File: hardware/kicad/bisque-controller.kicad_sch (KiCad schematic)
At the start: 49 parts, among them J1 USB-C, J2 5V_IN, J3 TC_K, J4 SSR, J5 DISPLAY, J6 NAV_SW, J7 AUX, Q1 AO3400A, Q2 AO3400A, SW1 RESET, SW2 BOOT, U1 ESP32-S3-WROOM-1-N8R2, U2 AMS1117-3.3, U3 MAX31855KASA+, U4 USBLC6-2SC6

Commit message: Replace pin headers with Molex KK-254 friction-lock headers
J5 (display), J6 (nav switch) and J7 (aux) switch from plain 2.54mm pin
headers to Molex KK-254 AE-6410 friction-lock headers, so each mating
housing is polarized and cannot be plugged in reversed. Pin positions are
unchanged (same 2.54mm row); the board was re-routed around the larger
oval pads and re-verified (ALL CHECKS PASS). Silk pin-name labels moved
out from under the deeper connector bodies, 3D renders updated with the
friction-lock body shape, BOM lists the headers plus mating housings and
crimp terminals.

Co-Authored-By: Claude Fable 5 <noreply@anthropic.com>
Claude-Session: https://claude.ai/code/session_017JbapEYPC7fC91erkTARYt
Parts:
- J5, J7: footprint Connector_PinHeader_2.54mm:PinHeader_1x08_P2.54mm_Vertical -> Connector_Molex:Molex_KK-254_AE-6410-08A_1x08_P2.54mm_Vertical
- J6: footprint Connector_PinHeader_2.54mm:PinHeader_1x06_P2.54mm_Vertical -> Connector_Molex:Molex_KK-254_AE-6410-06A_1x06_P2.54mm_Vertical
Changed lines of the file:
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@@
 			(effects (font (size 1.27 1.27)) (justify left))
 		)
-		(property "Footprint" "Connector_PinHeader_2.54mm:PinHeader_1x08_P2.54mm_Vertical" (at 39.37 214.63 0)
+		(property "Footprint" "Connector_Molex:Molex_KK-254_AE-6410-08A_1x08_P2.54mm_Vertical" (at 39.37 214.63 0)
 			(effects (font (size 1.27 1.27)) (hide yes))
 		)
@@
 			(effects (font (size 1.27 1.27)) (justify left))
 		)
-		(property "Footprint" "Connector_PinHeader_2.54mm:PinHeader_1x06_P2.54mm_Vertical" (at 76.2 214.63 0)
+		(property "Footprint" "Connector_Molex:Molex_KK-254_AE-6410-06A_1x06_P2.54mm_Vertical" (at 76.2 214.63 0)
 			(effects (font (size 1.27 1.27)) (hide yes))
 		)
@@
 			(effects (font (size 1.27 1.27)) (justify left))
 		)
-		(property "Footprint" "Connector_PinHeader_2.54mm:PinHeader_1x08_P2.54mm_Vertical" (at 111.76 214.63 0)
-			(effects (font (size 1.27 1.27)) (hide yes))
-		)
+		(property "Footprint" "Connector_Molex:Molex_KK-254_AE-6410-08A_1x08_P2.54mm_Vertical" (at 111.76 214.63 0)
+			(effects (font (size 1.27 1.27)) (hide yes))
+		)

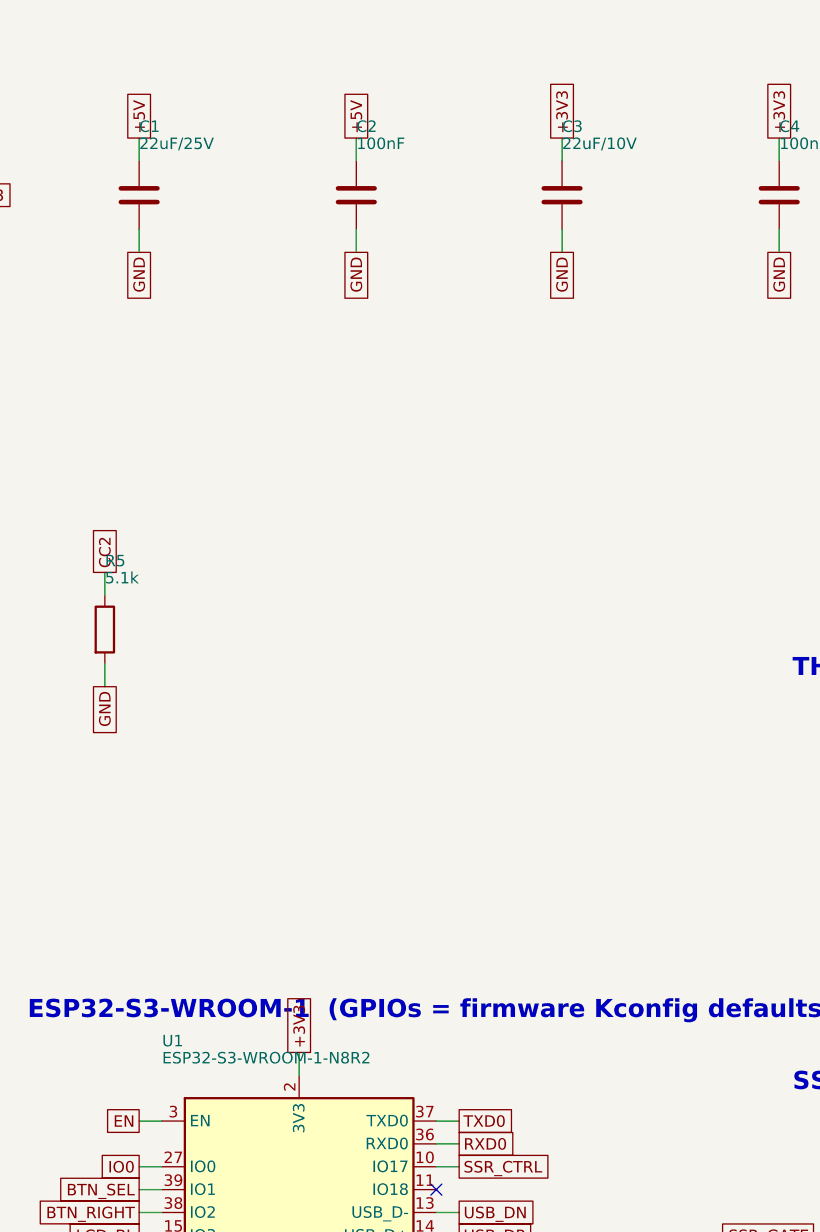
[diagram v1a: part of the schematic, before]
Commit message: Verify JLCPCB manufacturability, add assembly BOM/CPL export
- Confirm the board clears JLCPCB standard 2-layer capabilities with wide
  margins (0.25mm min track vs 0.127 limit, 0.6/0.3 vias, 0.3mm min
  drill, 100x80mm inside the cheapest <=100x100mm tier) — no upcharges.
- Fix U1 variant: firmware sdkconfig uses octal PSRAM and a 16MB OTA
  partition table, so the module must be ESP32-S3-WROOM-1-N16R8 (LCSC
  C2913202, in stock), not N8R2. IO35-37 were already NC on the board as
  octal PSRAM requires.
- Consolidate C1/C3 to one 22uF/25V 1206 part for BOM simplicity.
- New generator/gen_jlc.py emits jlcpcb/BOM.csv + CPL.csv with LCSC part
  numbers (verified ones marked; commodity parts flagged for confirmation
  in JLC's BOM matcher). Key parts verified in catalog: ESP32-S3 module,
  MAX31855KASA+T (C52028), USB-C TYPE-C-31-M-12 (C165948), AMS1117,
  AO3400A, SS34/SS14, 1N4148W and all passives as Basic parts.
- README: fabrication capability table, price expectations, and three
  assembly strategies (SMT-only recommended).

Co-Authored-By: Claude Fable 5 <noreply@anthropic.com>
Claude-Session: https://claude.ai/code/session_017JbapEYPC7fC91erkTARYt
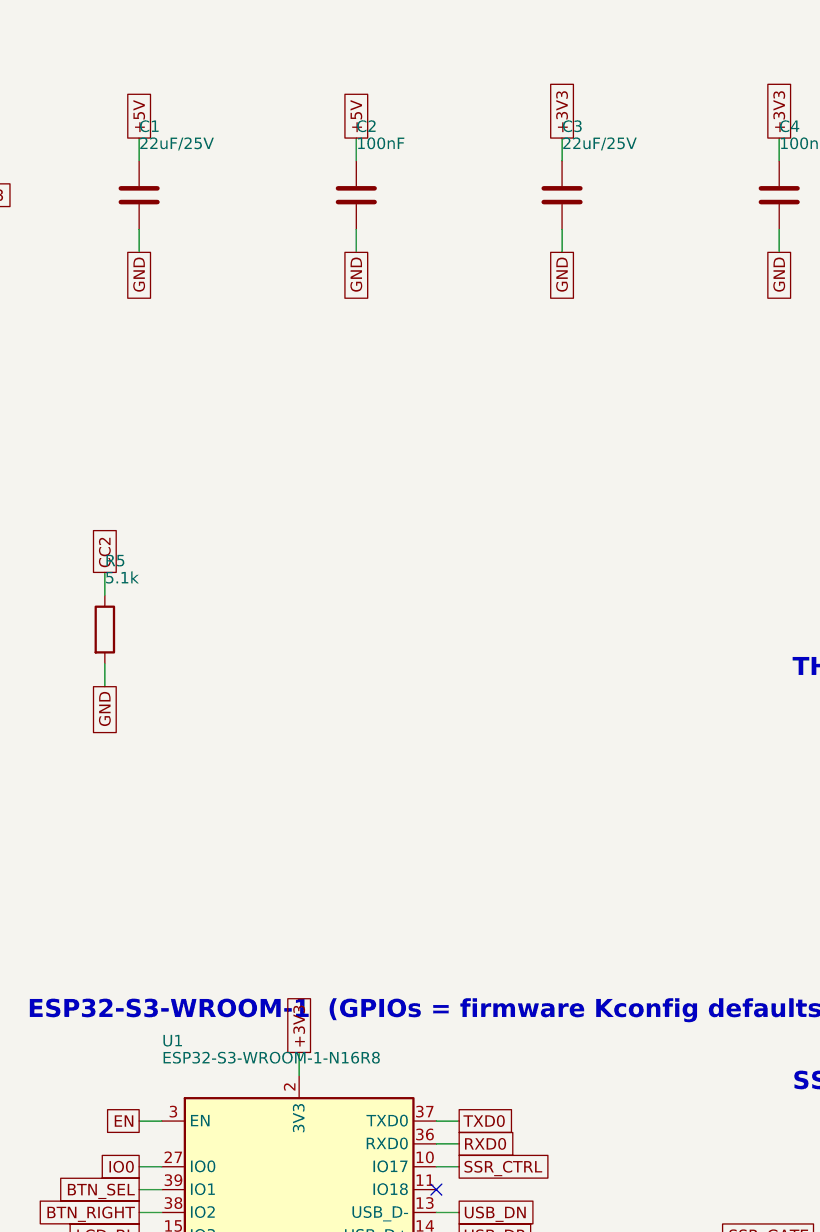
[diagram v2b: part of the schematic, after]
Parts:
- C3: value 22uF/10V -> 22uF/25V
- U1: value ESP32-S3-WROOM-1-N8R2 -> ESP32-S3-WROOM-1-N16R8
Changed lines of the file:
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@@
 			(effects (font (size 1.27 1.27)) (justify left))
 		)
-		(property "Value" "ESP32-S3-WROOM-1-N8R2" (at 154.94 135.25 0)
+		(property "Value" "ESP32-S3-WROOM-1-N16R8" (at 154.94 135.25 0)
 			(effects (font (size 1.27 1.27)) (justify left))
 		)
@@
 			(effects (font (size 1.27 1.27)) (justify left))
 		)
-		(property "Value" "22uF/10V" (at 199.39 33.65 0)
-			(effects (font (size 1.27 1.27)) (justify left))
-		)
+		(property "Value" "22uF/25V" (at 199.39 33.65 0)
+			(effects (font (size 1.27 1.27)) (justify left))
+		)

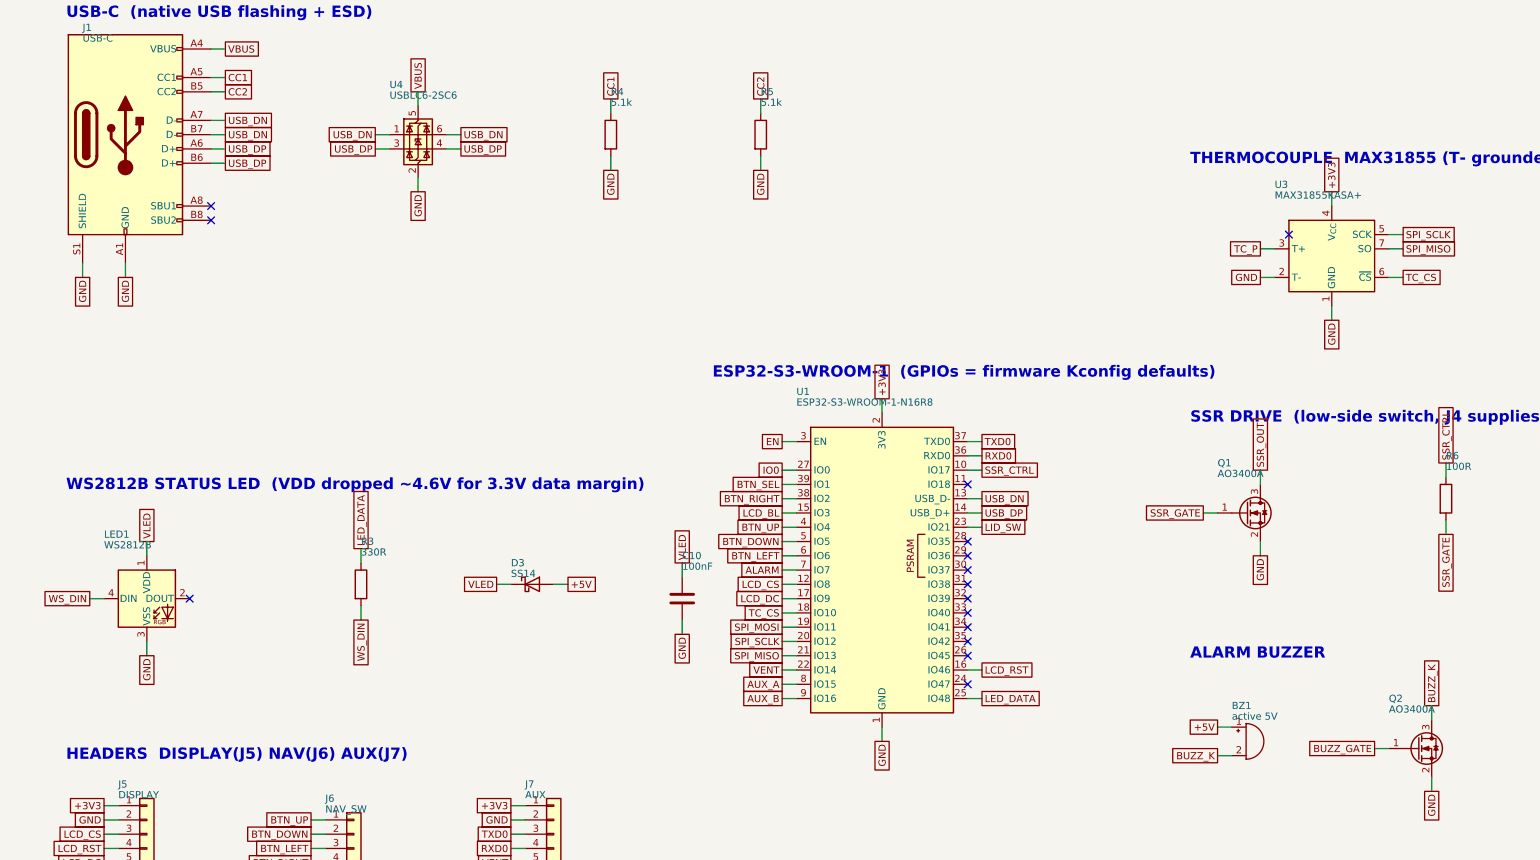
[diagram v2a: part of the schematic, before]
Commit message: Rebuild PCB and schematic through real KiCad (7.0.11)
KiCad is now installed in the build environment (Ubuntu universe; the
KiCad 9 PPA is blocked by network policy), so the project is rebuilt
through KiCad's own engine instead of hand-written file generation:

- generator/kicad_build.py constructs the board via the pcbnew Python
  API: footprints loaded from KiCad's installed system libraries, router
  obstacle model taken from the loaded pad geometry, tracks/vias/zones/
  silk added as real pcbnew objects, ground pours filled by KiCad's
  ZONE_FILLER, saved by pcbnew (KiCad 7 format, opens in 7/8/9).
- KiCad DRC (WriteDRCReport) runs as part of the build: ZERO errors,
  zero unconnected items (report committed). DRC drove real fixes my
  own checker had missed: module EP thermal vias upsized 0.2->0.3mm
  (keeps JLCPCB standard drill range), hole-to-hole clearance added to
  the router's via placement, solid pour connections where thermal
  spokes starved, explicit GND stubs routed for every SMD GND pad plus
  automatic pour-island healing (stitch via dropped into any isolated
  fill fragment), and a pre-seeded escape for U4's boxed-in GND pin.
- Schematic regenerated in KiCad 7 format from the system symbol
  libraries and validated by round-trip: kicad-cli exports the netlist
  and check_netlist.py diffs it against design.py - 42 nets, 0
  mismatches.
- Fabrication outputs exported with kicad-cli and committed: gerbers +
  Excellon drill + job file (gerbers/), schematic + board PDFs (pdf/).
- .kicad_pro rewritten by pcbnew as a native project with full rule
  severities; 2D/3D previews regenerated; README workflow updated.
  gen_pcb.py retained as a KiCad-free fallback generator.

Co-Authored-By: Claude Fable 5 <noreply@anthropic.com>
Claude-Session: https://claude.ai/code/session_017JbapEYPC7fC91erkTARYt
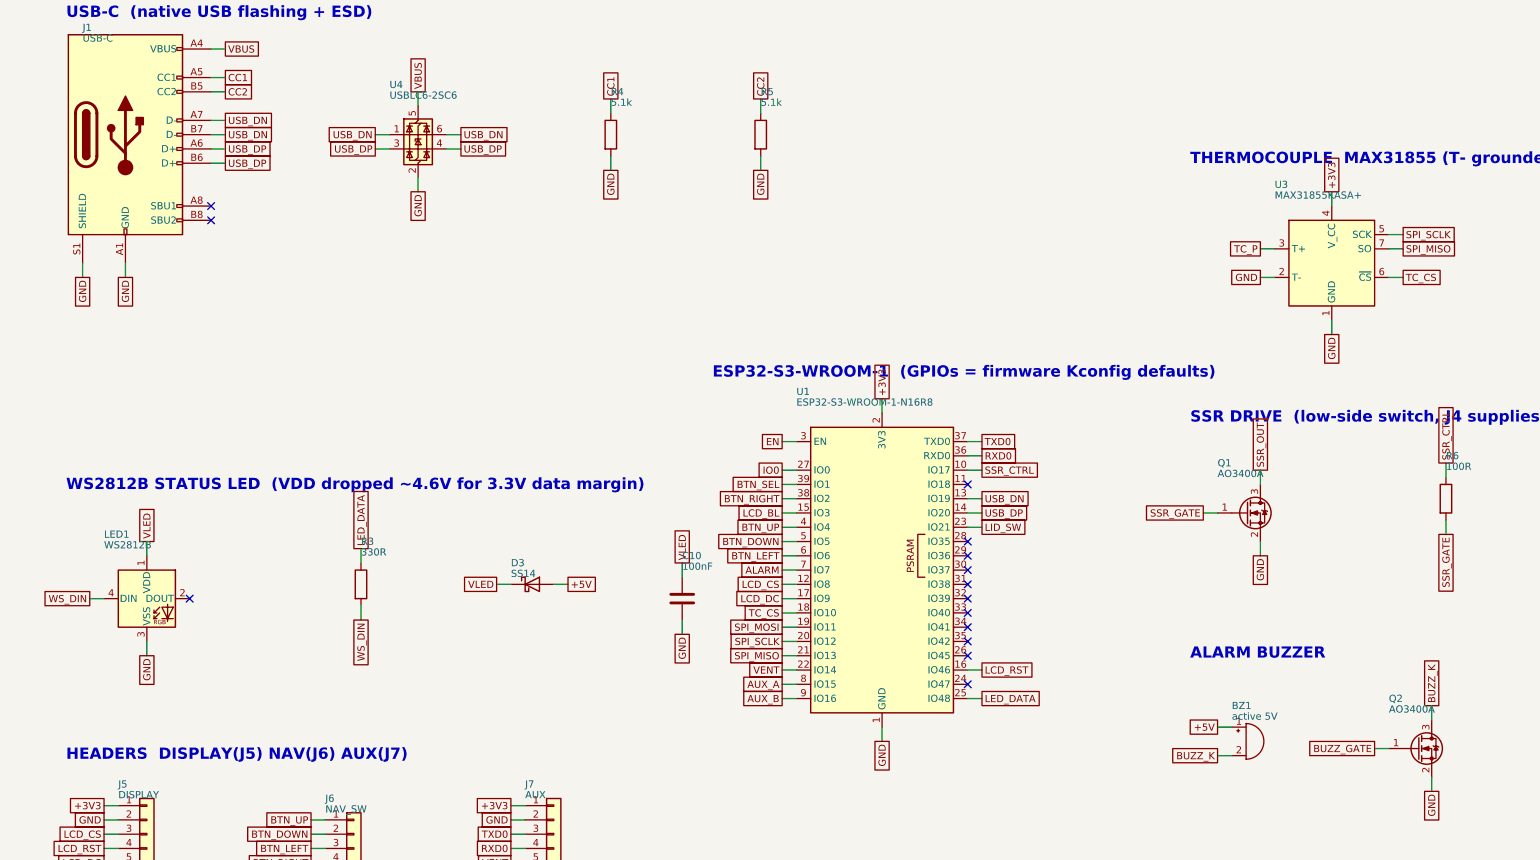
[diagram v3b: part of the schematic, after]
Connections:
- no-connect marks 15 -> 14
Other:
- moved on the sheet: U3

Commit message: Rebuild board with local KiCad 10.0.4; raytraced renders via kicad-cli
Recreates the PCB and all outputs with the locally installed KiCad 10:

- kicad_build.py is now version-adaptive: on KiCad 8+ the board is built
  via the pcbnew API, saved, then kicad-cli pcb drc --refill-zones
  --save-board fills the pours and runs DRC in one authentic pass (the
  v7 in-memory flow is kept for that generation). macOS standalone
  scripting fixes: wx.App bootstrap, PCB_IO_MGR.FindPlugin footprint
  loading, EDA_UNITS_MM, SetLocalZoneConnection.
- KiCad 10 library rename handled: the USB-C shield pin/pads are 'SH'
  (was 'S1' in <=9); design.py carries both aliases and the netlist
  round-trip normalizes them. Round-trip: 42 nets, 0 mismatches.
- KiCad 10 DRC: 0 errors, 0 unconnected, 16 cosmetic silk warnings
  (report committed). Independent geometry checker updated for the v10
  file format (name-referenced nets) - ALL CHECKS PASS.
- 3D renders are now genuine kicad-cli raytraces with official component
  models (generator/render-3d.sh); the three.js renderer remains as a
  KiCad-free fallback. Gerbers/drill/PDFs re-exported with kicad-cli 10.

Co-Authored-By: Claude Fable 5 <noreply@anthropic.com>
Claude-Session: https://claude.ai/code/session_017JbapEYPC7fC91erkTARYt
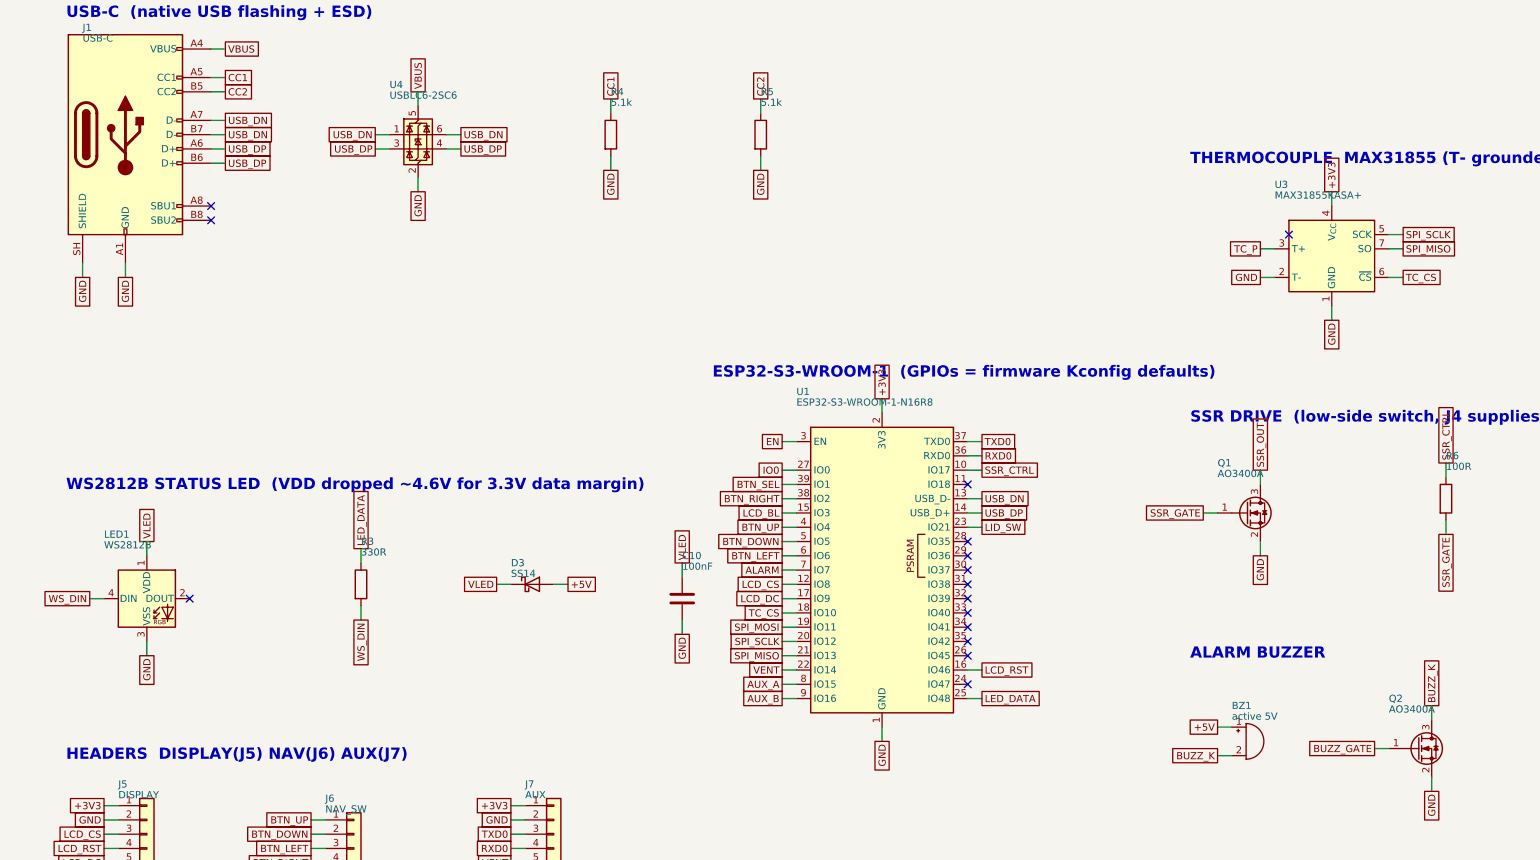
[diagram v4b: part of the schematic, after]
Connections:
- net GND: now also J1.SH (SHIELD); no longer J1.S1 (SHIELD)
- no-connect marks 14 -> 15
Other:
- moved on the sheet: U3
